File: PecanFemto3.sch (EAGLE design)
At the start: 37 parts, among them IC1 SPV1040T, IC3 EVA7M, IC4 SI4060/3, IC5 LPC824M201JHI33E, U1 TPS62203DBVT

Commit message: Routed parts
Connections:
- net CS_RADIO: now also IC5.PIO0_16; no longer IC5.PIO0_10/I2C0_SCL
- net IRQ: now also IC5.PIO0_24; no longer IC5.PIO0_25
- net MISO: now also IC5.PIO0_26; no longer IC5.PIO0_27
- net MOSI: now also IC5.PIO0_27; no longer IC5.PIO0_16
- net RADIO_SDN: now also IC5.PIO0_10/I2C0_SCL
- net SCK: now also IC5.PIO0_25; no longer IC5.PIO0_26
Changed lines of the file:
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@@
+</segment>
+<segment>
+<pinref part="IC5" gate="G$1" pin="PIO0_25"/>
+<wire x1="22.86" y1="15.24" x2="25.4" y2="15.24" width="0.1524" layer="91"/>
+<label x="25.4" y="15.24" size="1.27" layer="95" xref="yes"/>
+</segment>
+</net>
+<net name="SWCLK" class="0">
+<segment>
+<wire x1="88.9" y1="2.54" x2="101.6" y2="2.54" width="0.1524" layer="91"/>
+<label x="88.9" y="2.54" size="1.27" layer="95" rot="R180" xref="yes"/>
+<pinref part="JP1" gate="A" pin="7"/>
+</segment>
+<segment>
+<pinref part="IC5" gate="G$1" pin="SWCLK/PIO0_3/TCK"/>
+<wire x1="-43.18" y1="12.7" x2="-45.72" y2="12.7" width="0.1524" layer="91"/>
+<label x="-45.72" y="12.7" size="1.27" layer="95" rot="R180" xref="yes"/>
+</segment>
+</net>
+<net name="MOSI" class="0">
+<segment>
+<pinref part="IC4" gate="G$1" pin="14_SDI"/>
+<wire x1="172.72" y1="33.02" x2="170.18" y2="33.02" width="0.1524" layer="91"/>
+<label x="170.18" y="33.02" size="1.27" layer="95" rot="R180" xref="yes"/>
+</segment>
+<segment>
+<pinref part="IC5" gate="G$1" pin="PIO0_27"/>
+<wire x1="22.86" y1="20.32" x2="25.4" y2="20.32" width="0.1524" layer="91"/>
+<label x="25.4" y="20.32" size="1.27" layer="95" xref="yes"/>
+</segment>
+</net>
+<net name="MISO" class="0">
+<segment>
+<pinref part="IC4" gate="G$1" pin="13_SDO"/>
+<wire x1="170.18" y1="40.64" x2="172.72" y2="40.64" width="0.1524" layer="91"/>
+<label x="170.18" y="40.64" size="1.27" layer="95" rot="R180" xref="yes"/>
 </segment>
 <segment>
@@
 <wire x1="22.86" y1="17.78" x2="25.4" y2="17.78" width="0.1524" layer="91"/>
 <label x="25.4" y="17.78" size="1.27" layer="95" xref="yes"/>
-</segment>
-</net>
-<net name="SWCLK" class="0">
-<segment>
-<wire x1="88.9" y1="2.54" x2="101.6" y2="2.54" width="0.1524" layer="91"/>
-<label x="88.9" y="2.54" size="1.27" layer="95" rot="R180" xref="yes"/>
-<pinref part="JP1" gate="A" pin="7"/>
-</segment>
-<segment>
-<pinref part="IC5" gate="G$1" pin="SWCLK/PIO0_3/TCK"/>
-<wire x1="-43.18" y1="12.7" x2="-45.72" y2="12.7" width="0.1524" layer="91"/>
-<label x="-45.72" y="12.7" size="1.27" layer="95" rot="R180" xref="yes"/>
-</segment>
-</net>
-<net name="MOSI" class="0">
-<segment>
-<pinref part="IC4" gate="G$1" pin="14_SDI"/>
-<wire x1="172.72" y1="33.02" x2="170.18" y2="33.02" width="0.1524" layer="91"/>
-<label x="170.18" y="33.02" size="1.27" layer="95" rot="R180" xref="yes"/>
-</segment>
-<segment>
-<pinref part="IC5" gate="G$1" pin="PIO0_16"/>
-<wire x1="22.86" y1="22.86" x2="25.4" y2="22.86" width="0.1524" layer="91"/>
-<label x="25.4" y="22.86" size="1.27" layer="95" xref="yes"/>
-</segment>
-</net>
-<net name="MISO" class="0">
-<segment>
-<pinref part="IC4" gate="G$1" pin="13_SDO"/>
-<wire x1="170.18" y1="40.64" x2="172.72" y2="40.64" width="0.1524" layer="91"/>
-<label x="170.18" y="40.64" size="1.27" layer="95" rot="R180" xref="yes"/>
-</segment>
-<segment>
-<pinref part="IC5" gate="G$1" pin="PIO0_27"/>
-<wire x1="22.86" y1="20.32" x2="25.4" y2="20.32" width="0.1524" layer="91"/>
-<label x="25.4" y="20.32" size="1.27" layer="95" xref="yes"/>
 </segment>
 </net>
@@
 </segment>
 <segment>
+<pinref part="IC5" gate="G$1" pin="PIO0_16"/>
+<wire x1="22.86" y1="22.86" x2="25.4" y2="22.86" width="0.1524" layer="91"/>
+<label x="25.4" y="22.86" size="1.27" layer="95" xref="yes"/>
+</segment>
+</net>
+<net name="RADIO_SDN" class="0">
+<segment>
+<pinref part="IC4" gate="G$1" pin="1_SDN"/>
+<wire x1="264.16" y1="25.4" x2="266.7" y2="25.4" width="0.1524" layer="91"/>
+<label x="266.7" y="25.4" size="1.27" layer="95" xref="yes"/>
+</segment>
+<segment>
 <pinref part="IC5" gate="G$1" pin="PIO0_10/I2C0_SCL"/>
 <wire x1="22.86" y1="35.56" x2="25.4" y2="35.56" width="0.1524" layer="91"/>
 <label x="25.4" y="35.56" size="1.27" layer="95" xref="yes"/>
-</segment>
-</net>
-<net name="RADIO_SDN" class="0">
-<segment>
-<pinref part="IC4" gate="G$1" pin="1_SDN"/>
-<wire x1="264.16" y1="25.4" x2="266.7" y2="25.4" width="0.1524" layer="91"/>
-<label x="266.7" y="25.4" size="1.27" layer="95" xref="yes"/>
 </segment>
 </net>
@@
 </segment>
 <segment>
-<pinref part="IC5" gate="G$1" pin="PIO0_25"/>
-<wire x1="22.86" y1="15.24" x2="25.4" y2="15.24" width="0.1524" layer="91"/>
-<label x="25.4" y="15.24" size="1.27" layer="95" xref="yes"/>
-</segment>
-</net>
+<pinref part="IC5" gate="G$1" pin="PIO0_24"/>
+<wire x1="22.86" y1="12.7" x2="25.4" y2="12.7" width="0.1524" layer="91"/>
+<label x="25.4" y="12.7" size="1.27" layer="95" xref="yes"/>
+</segment>
+</net>

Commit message: Moved parts, updated libs, added pads, added programmer pins
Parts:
- removed ANTENNA, GND, PAD4: (no value), PecanFemto4:SMD2
- added ANT1, ANT2, ANT3: TP, testpad:TP
- added GND24, GND28, GND30, GPSANT, VBAT1, VSOL: (no value), PecanFemto4:SMD2
- renumbered PAD5 to GND29
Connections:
- removed net OUT3: JP1.4
- removed net OUT4: JP1.2
- net GND: now also GND24.P, GND28.P, GND30.P, JP1.4, JP1.7; no longer GND.P, JP1.10, JP1.11
- net N$1: now also GPSANT.P; no longer PAD4.P
- net N$3: now also ANT1.TP, ANT2.TP, ANT3.TP; no longer ANTENNA.P
- net OUT1: now also JP1.9; no longer JP1.8
- net OUT2: now also JP1.11; no longer JP1.6
- net RESET: now also JP1.10; no longer JP1.9
- net SWCLK: now also JP1.8; no longer JP1.7
- net SWDIO: now also JP1.6; no longer JP1.5
- net VBAT: now also VBAT1.P
- net VCC: now also JP1.2, JP1.5
- net VSOLAR: now also VSOL.P
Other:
- moved on the sheet: GND15

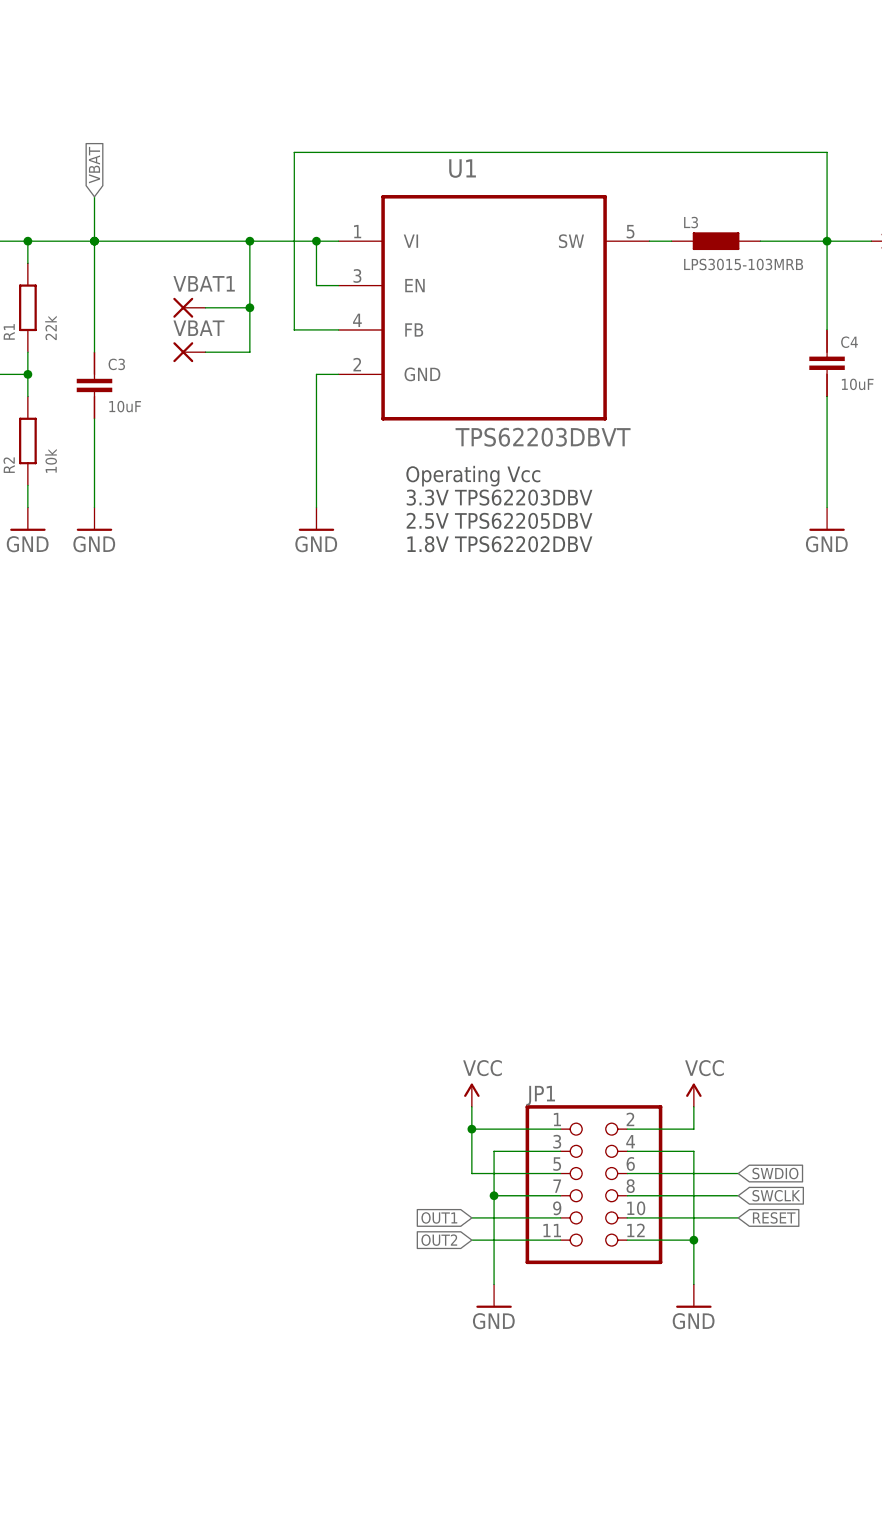
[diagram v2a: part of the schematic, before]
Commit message: Added LEDs, changed size of pinheader, moved parts
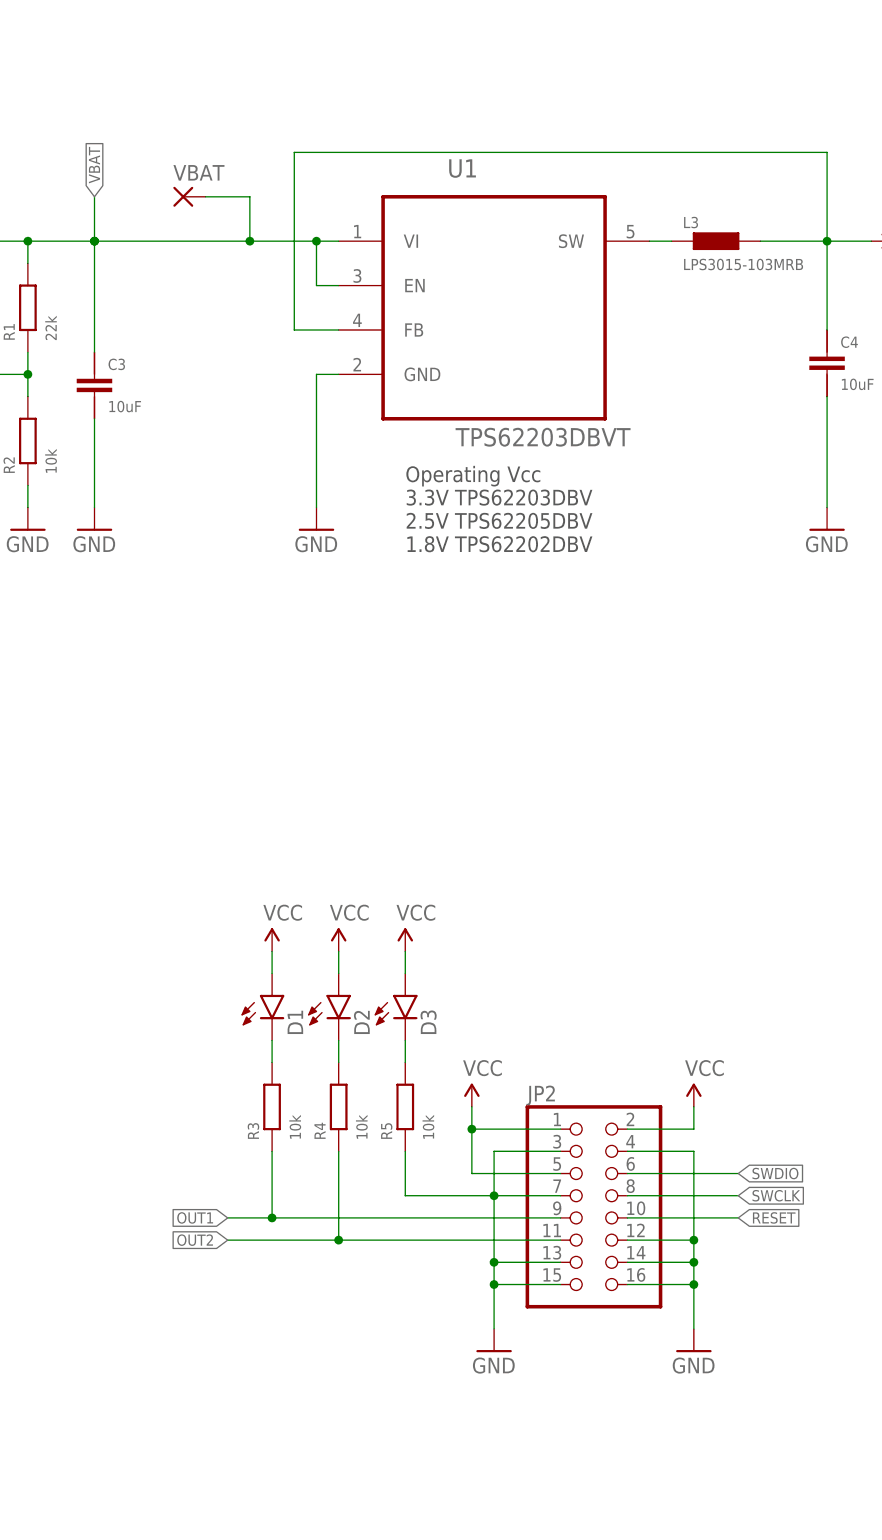
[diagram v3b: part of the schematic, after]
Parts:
- removed JP1: (no value), pinhead:PINHD-2X6
- removed VBAT1: (no value), PecanFemto4:SMD2
- added D1, D2, D3: (no value), SparkFun-LED:LED0603
- added JP2: (no value), pinhead:PINHD-2X8
- added R3, R4, R5: 10k, PecanPico6:RES-0402
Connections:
- new net N$11: D2.C, R4.2
- new net N$12: D3.C, R5.2
- new net N$8: D1.C, R3.2
- net GND: now also JP2.12, JP2.13, JP2.14, JP2.15, JP2.16, JP2.3, JP2.4, JP2.7, R5.1; no longer JP1.12, JP1.3, JP1.4, JP1.7
- net OUT1: now also JP2.9, R3.1; no longer JP1.9
- net OUT2: now also JP2.11, R4.1; no longer JP1.11
- net RESET: now also JP2.10; no longer JP1.10
- net SWCLK: now also JP2.8; no longer JP1.8
- net SWDIO: now also JP2.6; no longer JP1.6
- net VBAT: no longer VBAT1.P
- net VCC: now also D1.A, D2.A, D3.A, JP2.1, JP2.2, JP2.5; no longer JP1.1, JP1.2, JP1.5
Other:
- moved on the sheet: VBAT

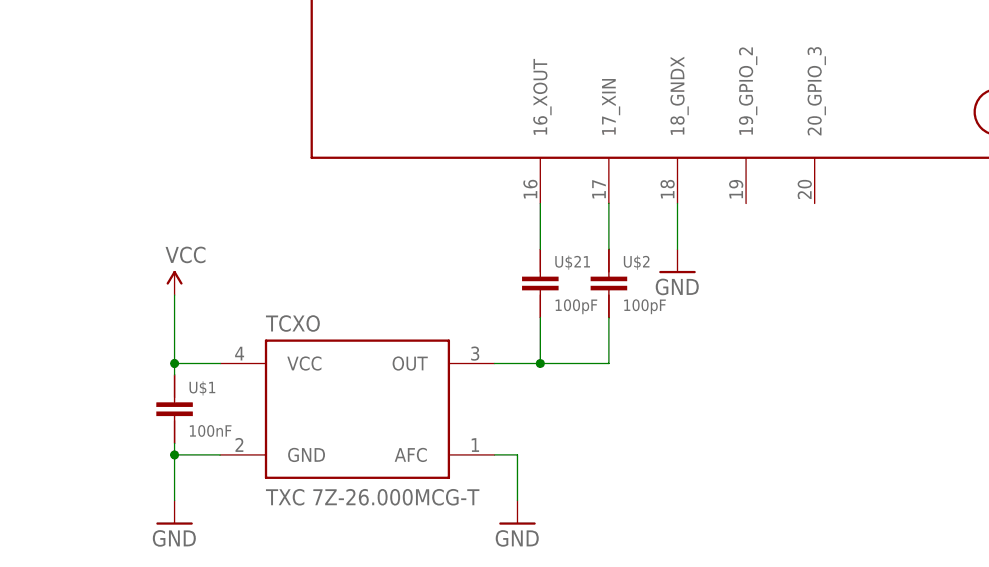
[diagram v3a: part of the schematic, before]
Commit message: Connected TCXO VCC to Si4464
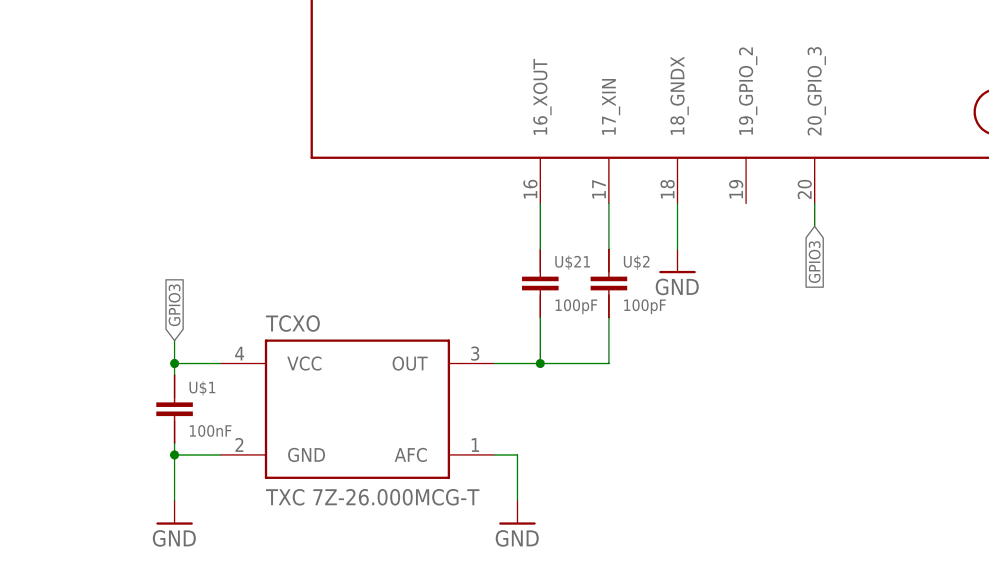
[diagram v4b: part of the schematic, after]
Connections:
- new net GPIO3: IC4.20_GPIO_3, TCXO.VCC, U$1.2
- net VCC: no longer TCXO.VCC, U$1.2
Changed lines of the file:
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@@
 <part name="GND8" library="SparkFun-Aesthetics" deviceset="GND" device=""/>
 <part name="GND14" library="SparkFun-Aesthetics" deviceset="GND" device=""/>
-<part name="SUPPLY5" library="SparkFun-Aesthetics" deviceset="VCC" device=""/>
 <part name="SUPPLY6" library="SparkFun-Aesthetics" deviceset="VCC" device=""/>
 <part name="U$21" library="sven" deviceset="CAP-0402" device="" value="100pF"/>
@@
 <instance part="GND8" gate="1" x="218.44" y="-12.7"/>
 <instance part="GND14" gate="1" x="185.42" y="93.98" rot="R180"/>
-<instance part="SUPPLY5" gate="G$1" x="162.56" y="-15.24"/>
 <instance part="SUPPLY6" gate="G$1" x="-48.26" y="40.64"/>
 <instance part="U$21" gate="G$1" x="203.2" y="-12.7"/>
@@
 </segment>
 <segment>
-<pinref part="SUPPLY5" gate="G$1" pin="VCC"/>
-<wire x1="162.56" y1="-22.86" x2="162.56" y2="-15.24" width="0.1524" layer="91"/>
-<wire x1="167.64" y1="-22.86" x2="162.56" y2="-22.86" width="0.1524" layer="91"/>
-<pinref part="U$1" gate="G$1" pin="2"/>
-<wire x1="162.56" y1="-24.13" x2="162.56" y2="-22.86" width="0.1524" layer="91"/>
-<junction x="162.56" y="-22.86"/>
-<pinref part="TCXO" gate="TCXO" pin="VCC"/>
-</segment>
-<segment>
 <wire x1="76.2" y1="101.6" x2="71.12" y2="101.6" width="0.1524" layer="91"/>
 <wire x1="71.12" y1="101.6" x2="71.12" y2="121.92" width="0.1524" layer="91"/>
@@
 </segment>
 </net>
+<net name="GPIO3" class="0">
+<segment>
+<pinref part="IC4" gate="G$1" pin="20_GPIO_3"/>
+<wire x1="233.68" y1="-5.08" x2="233.68" y2="-7.62" width="0.1524" layer="91"/>
+<label x="233.68" y="-7.62" size="1.27" layer="95" rot="R270" xref="yes"/>
+</segment>
+<segment>
+<wire x1="167.64" y1="-22.86" x2="162.56" y2="-22.86" width="0.1524" layer="91"/>
+<pinref part="U$1" gate="G$1" pin="2"/>
+<wire x1="162.56" y1="-24.13" x2="162.56" y2="-22.86" width="0.1524" layer="91"/>
+<pinref part="TCXO" gate="TCXO" pin="VCC"/>
+<wire x1="162.56" y1="-22.86" x2="162.56" y2="-20.32" width="0.1524" layer="91"/>
+<junction x="162.56" y="-22.86"/>
+<label x="162.56" y="-20.32" size="1.27" layer="95" rot="R90" xref="yes"/>
+</segment>
+</net>

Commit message: Connected V_USB and RTC_I to GND
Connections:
- net GND: now also IC3.RTC_I, IC3.V_USB
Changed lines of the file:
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@@
 <part name="D3" library="SparkFun-LED" deviceset="LED" device="0603"/>
 <part name="SUPPLY11" library="SparkFun-Aesthetics" deviceset="VCC" device=""/>
+<part name="GND13" library="SparkFun-Aesthetics" deviceset="GND" device=""/>
 </parts>
 <sheets>
@@
 <instance part="D3" gate="G$1" x="83.82" y="25.4"/>
 <instance part="SUPPLY11" gate="G$1" x="83.82" y="30.48"/>
+<instance part="GND13" gate="1" x="289.56" y="165.1"/>
 </instances>
 <busses>
@@
 <pinref part="GND31" gate="1" pin="GND"/>
 </segment>
-</net>
+<segment>
+<pinref part="GND13" gate="1" pin="GND"/>
+<wire x1="289.56" y1="167.64" x2="289.56" y2="170.18" width="0.1524" layer="91"/>
+<pinref part="IC3" gate="G$1" pin="V_USB"/>
+<wire x1="289.56" y1="170.18" x2="289.56" y2="177.8" width="0.1524" layer="91"/>
+<wire x1="289.56" y1="177.8" x2="294.64" y2="177.8" width="0.1524" layer="91"/>
+<pinref part="IC3" gate="G$1" pin="RTC_I"/>
+<wire x1="294.64" y1="170.18" x2="289.56" y2="170.18" width="0.1524" layer="91"/>
+<junction x="289.56" y="170.18"/>
+</segment>
+</net>

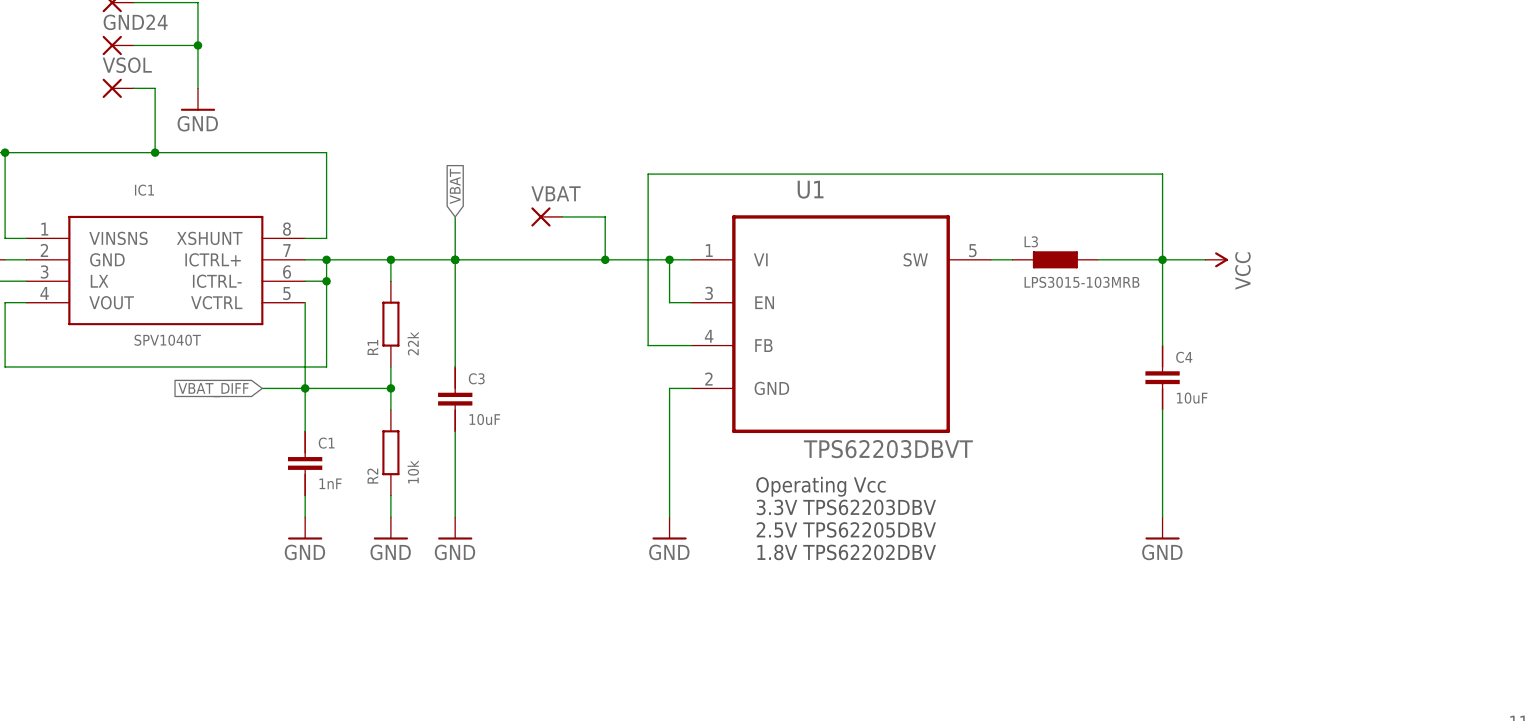
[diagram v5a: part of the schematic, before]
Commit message: Moved parts around
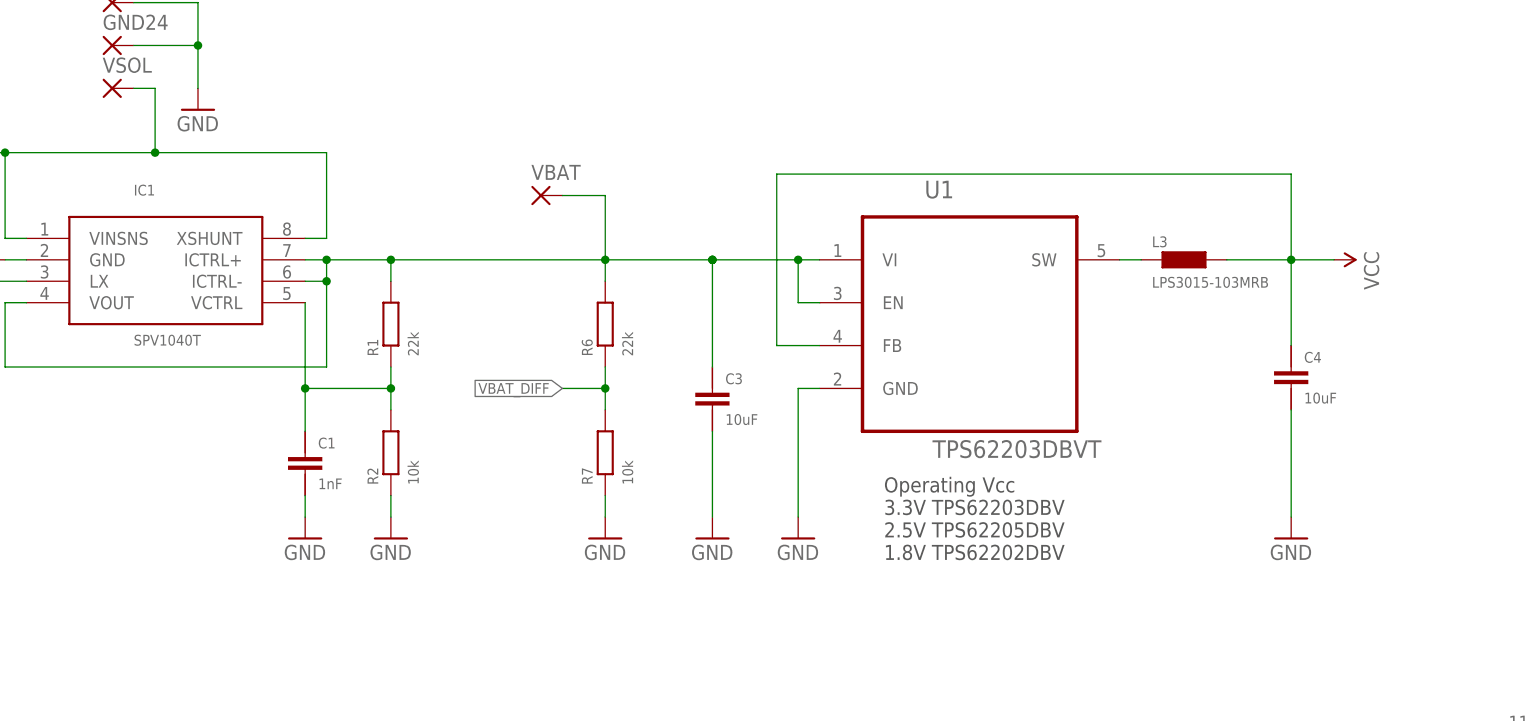
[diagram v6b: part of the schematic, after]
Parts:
- added R6: 22k, PecanPico6:RES-0402
- added R7: 10k, PecanPico6:RES-0402
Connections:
- new net N$20: C1.2, IC1.VCTRL, R1.1, R2.2
- net GND: now also R7.1
- net VBAT: now also R6.2
- net VBAT_DIFF: now also R6.1, R7.2; no longer C1.2, IC1.VCTRL, R1.1, R2.2
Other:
- moved on the sheet: C3, C4, L3, U1, VBAT
